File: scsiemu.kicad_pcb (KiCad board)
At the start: 2 copper layers, 65 x 41.7 mm, 38 parts, among them J1 RasPi, J2 SCSI, J3 USB_POWER, J4 POWER 5V, J5 I2C, U1 74LS641-1, U2 74LS641-1, U3 74LS641-1, U4 74LS641-1

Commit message: update libs update PCBs update schematic
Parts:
- removed REF** (x6): MountingHole_2.2mm_M2, MountingHole:MountingHole_2.2mm_M2
- removed RN10, RN5, RN7, RN8: 220, Resistor_SMD:R_Cat16-8
- removed RN11, RN6, RN9: 330, Resistor_SMD:R_Cat16-8
- added C10: 10u, Capacitor_SMD:C_1206_3216Metric_Pad1.42x1.75mm_HandSolder, B.Cu at (183.9, 64.0)
- added C11: 10u, Capacitor_SMD:C_1206_3216Metric_Pad1.42x1.75mm_HandSolder, B.Cu at (155.6, 64.3)
- added C6: 10u, Capacitor_SMD:C_1206_3216Metric_Pad1.42x1.75mm_HandSolder, F.Cu at (176.8, 49.1)
- added C7: 2.2u, Capacitor_SMD:C_0603_1608Metric_Pad1.05x0.95mm_HandSolder, F.Cu at (176.4, 61.6)
- added C8: 10u, Capacitor_SMD:C_1206_3216Metric_Pad1.42x1.75mm_HandSolder, F.Cu at (165.7, 48.0)
- added C9: 2.2u, Capacitor_SMD:C_0603_1608Metric_Pad1.05x0.95mm_HandSolder, F.Cu at (173.2, 51.7)
- added D2: SBD, local_lib:D_SOD-123_HandSoldering, F.Cu at (120.1, 57.2)
- added J6: AT Power 5V (171826-4), local_lib:Molex_171826-4, F.Cu at (119.6, 49.8)
- added J7: I2C Ext, Connector_JST:JST_XH_B6B-XH-A_1x06_P2.50mm_Vertical, F.Cu at (174.0, 68.8)
- added J8: AT Power 5V (641737-1), local_lib:TE_641737-1, F.Cu at (122.2, 35.4)
- added LED2: LED ACT, LED_SMD:LED_0603_1608Metric_Pad1.05x0.95mm_HandSolder, F.Cu at (183.7, 68.4)
- added MH1: Raspi Mount, MountingHole:MountingHole_2.2mm_M2, F.Cu at (138.5, 100.2)
- added MH10: Raspi Mount, MountingHole:MountingHole_2.2mm_M2, F.Cu at (138.5, 126.2)
- added MH2: Raspi Mount, MountingHole:MountingHole_2.2mm_M2, F.Cu at (138.5, 77.2)
- added MH3: Raspi Mount, MountingHole:MountingHole_2.2mm_M2, F.Cu at (196.5, 77.2)
- added MH4: Raspi Mount, MountingHole:MountingHole_2.2mm_M2, F.Cu at (196.5, 100.2)
- added MH5: HDD Mount, MountingHole:MountingHole_3.5mm, F.Cu at (112.0, 57.0)
- added MH6: HDD Mount, MountingHole:MountingHole_3.5mm, F.Cu at (112.0, 133.2)
- added MH7: HDD Mount, MountingHole:MountingHole_3.5mm, F.Cu at (207.2, 57.0)
- added MH8: HDD Mount, MountingHole:MountingHole_3.5mm, F.Cu at (207.2, 133.2)
- added MH9: Raspi Mount, MountingHole:MountingHole_2.2mm_M2, F.Cu at (196.5, 126.2)
- added R2: 2.2k, Resistor_SMD:R_0603_1608Metric_Pad1.05x0.95mm_HandSolder, F.Cu at (125.3, 59.9)
- added R3: 2.7k, Resistor_SMD:R_0603_1608Metric_Pad1.05x0.95mm_HandSolder, F.Cu at (125.4, 57.8)
- added U5: DS2105Z, Package_SO:SOIC-16_3.9x9.9mm_P1.27mm, F.Cu at (181.6, 56.6)
- added U6: DS2105Z, Package_SO:SOIC-16_3.9x9.9mm_P1.27mm, F.Cu at (168.0, 55.9)
- added U7: TL2218-285, Package_SO:TSSOP-20_4.4x6.5mm_P0.65mm, B.Cu at (190.1, 66.5)
- added U8: TL2218-285, Package_SO:TSSOP-20_4.4x6.5mm_P0.65mm, B.Cu at (147.2, 64.3)
- C1, C4: value 0.1u JB -> 0.1u; moved to F.Cu
- C2: value 0.1u JB -> 0.1u
- C3: value 0.1u JIS B -> 0.1u; moved to F.Cu
- C5: value 10u JB -> 10u; moved to F.Cu
- D1: footprint cd_device:D_SOD-123_HandSoldering -> local_lib:D_SOD-123_HandSoldering; moved to F.Cu
- F1, FL1, FL2, R1, U1, U2, U3, U4: moved to F.Cu
- F2: value 1A -> 2A; moved to F.Cu
- J2: footprint local_lib:DSUB50P -> Connector_PinHeader_2.54mm:PinHeader_2x25_P2.54mm_Horizontal
- J4: footprint Connector_JST:JST_PH_S2B-PH-K_1x02_P2.00mm_Horizontal -> Connector_JST:JST_XH_B2B-XH-A_1x02_P2.50mm_Vertical
- J5: value I2C -> POWER 5V; footprint Connector_JST:JST_PH_S3B-PH-K_1x03_P2.00mm_Horizontal -> Connector_JST:JST_XH_B2B-XH-A_1x02_P2.50mm_Vertical
- moved J1 85.3 mm to (191.6, 78.4), turned to 270 degrees
- moved LED1 83.9 mm to (180.1, 67.1), turned to 270 degrees
- moved R1 80.5 mm to (179.5, 64.2), turned to 90 degrees
- moved FL1 78.2 mm to (191.8, 83.1), turned to 270 degrees
- moved C5 55.8 mm to (162.1, 104.4), turned to 270 degrees
- moved U1 55.4 mm to (193.3, 116.6), turned to 0 degrees
- moved U2 55.0 mm to (186.4, 100.1), turned to 0 degrees
- moved C2 53.7 mm to (191.3, 91.7), turned to 90 degrees
- moved C1 50.1 mm to (198.1, 108.0), turned to 90 degrees
- moved J3 46.8 mm to (124.8, 135.6), turned to 0 degrees
- moved RN1 41.8 mm to (173.2, 101.3), turned to 180 degrees
- moved RN4 39.4 mm to (175.8, 116.1), turned to 180 degrees
- moved C3 34.6 mm to (148.3, 103.9), turned to 90 degrees
- moved F2 33.8 mm to (126.5, 66.7)
- moved RN3 33.0 mm to (153.4, 91.4), turned to 0 degrees
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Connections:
- D1 pad 2: VCC -> /5V_DC
- F2 pad 1: Net-(F2-Pad1) -> /5V_DC
- F2 pad 2: Net-(F2-Pad2) -> Net-(D2-Pad1)
- FL2 pad 3: Net-(F2-Pad1) -> /5V_DC
- J1 pad 2: Net-(F2-Pad1) -> /5V_DC
- J1 pad 21: Net-(J1-Pad21) -> /AT_POWER_ON
- J1 pad 27: Net-(J1-Pad27) -> /EXT1
- J1 pad 28: Net-(J1-Pad28) -> /EXT2
- J1 pad 4: Net-(F2-Pad1) -> /5V_DC
- J2 pad 10: GND -> /S_D4
- J2 pad 12: GND -> /S_D5
- J2 pad 14: GND -> /S_D6
- J2 pad 16: GND -> /S_D7
- J2 pad 18: GND -> /S_DP
- J2 pad 2: GND -> /S_D0
- J2 pad 25: GND -> Net-(J2-Pad25)
- J2 pad 26: /S_D0 -> Net-(F1-Pad1)
- J2 pad 27: /S_D1 -> GND
- J2 pad 28: /S_D2 -> GND
- J2 pad 29: /S_D3 -> GND
- J2 pad 30: /S_D4 -> GND
- J2 pad 31: /S_D5 -> GND
- J2 pad 32: /S_D6 -> /S_ATN
- J2 pad 33: /S_D7 -> GND
- J2 pad 34: /S_DP -> Net-(J2-Pad34)
- J2 pad 36: GND -> /S_BSY
- J2 pad 38: Net-(F1-Pad1) -> /S_ACK
- J2 pad 4: GND -> /S_D1
- J2 pad 40: GND -> /S_RST
- J2 pad 41: Net-(J2-Pad41) -> GND
- J2 pad 42: GND -> /S_MSG
- J2 pad 43: Net-(J2-Pad43) -> GND
- J2 pad 44: Net-(J2-Pad44) -> /S_SEL
- J2 pad 45: Net-(J2-Pad45) -> GND
- J2 pad 46: Net-(J2-Pad46) -> /S_CD
- J2 pad 47: Net-(J2-Pad47) -> GND
- J2 pad 48: Net-(J2-Pad48) -> /S_REQ
- J2 pad 49: Net-(J2-Pad49) -> GND
- J2 pad 50: Net-(J2-Pad50) -> /S_IO
- J2 pad 6: GND -> /S_D2
- J2 pad 8: GND -> /S_D3
- J3 pad 1: Net-(F2-Pad2) -> Net-(D2-Pad1)
- J4 pad 1: Net-(F2-Pad2) -> GND
- J4 pad 2: GND -> Net-(D2-Pad1)
- J5 pad 2: /I2C_SCL -> Net-(D2-Pad1)
- RN1 pad 3: Net-(RN1-Pad3) -> /SEL
- RN1 pad 4: Net-(RN1-Pad4) -> /RST
- RN1 pad 5: /ATN -> Net-(RN1-Pad5)
- RN1 pad 6: /RST -> Net-(RN1-Pad6)
- RN1 pad 8: /SEL -> /ATN
- RN2 pad 8: /DP -> /D0
- RN3 pad 1: /D3 -> /DP
- RN3 pad 2: /D1 -> /D7
- RN3 pad 3: /D0 -> /D6
- RN3 pad 4: /D2 -> /D5
- RN3 pad 5: /D5 -> /D4
- RN3 pad 6: /D6 -> /D3
- RN3 pad 7: /D4 -> /D2
- RN3 pad 8: /D7 -> /D1
- RN4 pad 4: /BSY -> /IO
- RN4 pad 5: /MSG -> /REQ
- RN4 pad 7: /REQ -> /MSG
- RN4 pad 8: /IO -> /BSY
- U1 pad 14: Net-(J2-Pad43) -> /S_IO
- U1 pad 15: Net-(J2-Pad46) -> /S_REQ
- U1 pad 16: Net-(J2-Pad48) -> /S_CD
- U1 pad 17: Net-(J2-Pad49) -> /S_MSG
- U1 pad 18: Net-(J2-Pad50) -> /S_BSY
- U1 pad 2: /IO -> /BSY
- U1 pad 3: /REQ -> /MSG
- U1 pad 5: /MSG -> /REQ
- U1 pad 6: /BSY -> /IO
- U2 pad 13: Net-(RN5-Pad3) -> /S_SEL
- U2 pad 14: Net-(RN5-Pad4) -> /S_RST
- U2 pad 15: Net-(J2-Pad41) -> Net-(U2-Pad15)
- U2 pad 16: Net-(J2-Pad45) -> Net-(U2-Pad16)
- U2 pad 17: Net-(J2-Pad44) -> /S_ACK
- U2 pad 18: Net-(J2-Pad47) -> /S_ATN
- U2 pad 2: /SEL -> /ATN
- U2 pad 4: /RST -> Net-(RN1-Pad6)
- U2 pad 5: /ATN -> Net-(RN1-Pad5)
- U2 pad 6: Net-(RN1-Pad4) -> /RST
- U2 pad 7: Net-(RN1-Pad3) -> /SEL
- U3 pad 11: /DP -> /D0
- U3 pad 9: /S_DP -> /S_D0
- U4 pad 11: /D7 -> /D1
- U4 pad 12: /D4 -> /D2
- U4 pad 13: /D6 -> /D3
- U4 pad 14: /D5 -> /D4
- U4 pad 15: /D2 -> /D5
- U4 pad 16: /D0 -> /D6
- U4 pad 17: /D1 -> /D7
- U4 pad 18: /D3 -> /DP
- U4 pad 2: /S_D3 -> /S_DP
- U4 pad 3: /S_D1 -> /S_D7
- U4 pad 4: /S_D0 -> /S_D6
- U4 pad 5: /S_D2 -> /S_D5
- U4 pad 6: /S_D5 -> /S_D4
- U4 pad 7: /S_D6 -> /S_D3
- U4 pad 8: /S_D4 -> /S_D2
- U4 pad 9: /S_D7 -> /S_D1
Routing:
- net /S_BSY: track 0.00 -> 120.0 mm, vias 0 -> 3
- net VCC: track 132.8 -> 14.9 mm, vias 4 -> 0
- net /S_REQ: track 0.00 -> 111.5 mm, vias 0 -> 2
- net /S_IO: track 0.00 -> 109.5 mm, vias 0 -> 2
- net /S_CD: track 0.00 -> 102.4 mm, vias 0 -> 1
- net /S_SEL: track 0.00 -> 101.5 mm, vias 0 -> 2
- net GND: track 100.9 -> 0.00 mm, vias 55 -> 33
- net /S_ACK: track 0.00 -> 99.8 mm, vias 0 -> 2
- net /S_MSG: track 0.00 -> 99.7 mm, vias 0 -> 1
- net /S_RST: track 0.00 -> 94.3 mm, vias 0 -> 1
- net /S_ATN: track 0.00 -> 89.8 mm, vias 0 -> 1
- net Net-(D2-Pad1): track 0.00 -> 81.3 mm
- net /5V_DC: track 0.00 -> 70.3 mm
- net /S_D0: track 12.7 -> 82.5 mm, vias 1 -> 0
- net /DTD: track 91.3 -> 26.3 mm, vias 3 -> 0
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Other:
- board size 65 x 41.7 mm -> 100 x 99 mm
- net class Default: clearance 0.2 -> 0.25; via_drill 0.4 -> 0.3
- net class LV added: clearance 0.2, trace_width 0.2, via_dia 0.7, via_drill 0.3
- rule trace_clearance: 0.2 -> 0.25
- board text added: "ATX POWER 5V"
- board text removed: "*"
- board text removed: "+"
- board text removed: "D+"
- board text removed: "D-"
- board text removed: "GND"
- board text removed: "ID"
- board text removed: "SDA|SCL|G"

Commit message: update track
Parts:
- added R4: 1k, Resistor_SMD:R_0603_1608Metric_Pad1.05x0.95mm_HandSolder, F.Cu at (128.0, 52.9)
- LED1: value LED ACT -> LED PWR; footprint LED_THT:LED_D3.0mm -> LED_SMD:LED_0603_1608Metric_Pad1.05x0.95mm_HandSolder
- moved LED1 51.6 mm to (130.4, 52.9)
- moved C5 9.88 mm to (152.2, 103.1), turned to 90 degrees
- moved LED2 2.69 mm to (181.0, 68.5)
- moved RN2 1.35 mm to (151.0, 111.4)
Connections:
- LED1 pad 2: /ACT -> /5V_DC
- LED2 pad 1: Net-(LED1-Pad1) -> Net-(LED2-Pad1)
- R1 pad 1: Net-(LED1-Pad1) -> Net-(LED2-Pad1)
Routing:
- net VCC: track 14.9 -> 200.3 mm, vias 0 -> 2
- net VEE: track 0.00 -> 155.6 mm, vias 0 -> 5
- net /RST: track 0.00 -> 74.1 mm
- net /D0: track 0.00 -> 72.1 mm, vias 0 -> 4
- net /BSY: track 0.00 -> 71.8 mm, vias 0 -> 2
- net /IO: track 0.00 -> 68.3 mm, vias 0 -> 2
- net /TAD: track 0.00 -> 60.4 mm, vias 0 -> 2
- net /MSG: track 0.00 -> 57.8 mm, vias 0 -> 2
- net /CD: track 0.00 -> 56.9 mm, vias 0 -> 2
- net /ACK: track 0.00 -> 56.9 mm, vias 0 -> 2
- net /REQ: track 0.00 -> 55.0 mm
- net /D4: track 0.00 -> 50.5 mm, vias 0 -> 1
- net /DTD: track 26.3 -> 74.6 mm, vias 0 -> 1
- net /D5: track 0.00 -> 47.9 mm, vias 0 -> 1
- net /ATN: track 0.00 -> 46.5 mm
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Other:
- board text added: "SCSI emu v1"
- board text removed: "SCSI"

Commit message: add tracks more
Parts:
- moved C11 18.9 mm to (149.6, 46.4), turned to 180 degrees
- moved U8 13.2 mm to (148.4, 51.1), turned to 180 degrees
- moved C8 1.88 mm to (167.6, 47.8)
- moved C6 1.83 mm to (178.5, 48.5)
- moved C9 1.04 mm to (173.2, 50.6)
- moved U6 0.32 mm to (168.1, 55.6)
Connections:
- U6 pad 11: Net-(U6-Pad11) -> /S_D0
- U6 pad 12: Net-(U6-Pad12) -> /S_D2
- U6 pad 13: Net-(U6-Pad13) -> /S_D4
- U6 pad 14: Net-(U6-Pad14) -> /S_D7
- U6 pad 2: Net-(U6-Pad2) -> /S_DP
- U6 pad 3: Net-(U6-Pad3) -> /S_D6
- U6 pad 4: Net-(U6-Pad4) -> /S_D5
- U6 pad 5: Net-(U6-Pad5) -> /S_D3
- U6 pad 6: Net-(U6-Pad6) -> /S_D1
- U8 pad 13: Net-(U8-Pad13) -> /S_D3
- U8 pad 14: Net-(U8-Pad14) -> /S_D2
- U8 pad 16: Net-(U8-Pad16) -> /S_D1
- U8 pad 17: Net-(U8-Pad17) -> /S_D0
- U8 pad 4: Net-(U8-Pad4) -> /S_DP
- U8 pad 5: Net-(U8-Pad5) -> /S_D7
- U8 pad 6: Net-(U8-Pad6) -> /S_D6
- U8 pad 7: Net-(U8-Pad7) -> /S_D5
- U8 pad 8: Net-(U8-Pad8) -> /S_D4
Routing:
- net VCC: track 200.3 -> 283.8 mm, vias 2 -> 4
- net /S_D0: track 82.5 -> 128.6 mm, vias 0 -> 2
- net GND: track 30.4 -> 72.1 mm, vias 121 -> 179
- net /S_D2: track 62.4 -> 99.8 mm, vias 0 -> 2
- net /S_D1: track 63.1 -> 96.8 mm, vias 0 -> 2
- net /S_D4: track 61.2 -> 86.0 mm, vias 0 -> 2
- net /S_D7: track 59.8 -> 83.5 mm, vias 0 -> 2
- net /S_D3: track 61.9 -> 84.4 mm, vias 0 -> 2
- net /AT_POWER_ON: track 41.3 -> 61.8 mm, vias 1 -> 3
- net /S_DP: track 59.3 -> 76.3 mm, vias 0 -> 1
- net /S_D5: track 60.5 -> 76.7 mm, vias 0 -> 2
- net /S_D6: track 60.1 -> 75.4 mm, vias 0 -> 2
- net Net-(C9-Pad1): track 0.00 -> 13.1 mm
- net /5V_DC: track 111.9 -> 118.7 mm
- net /AT_5V_DC: track 20.2 -> 25.0 mm
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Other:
- board text added: "SCSI emu v2"
- board text removed: "SCSI emu v1"

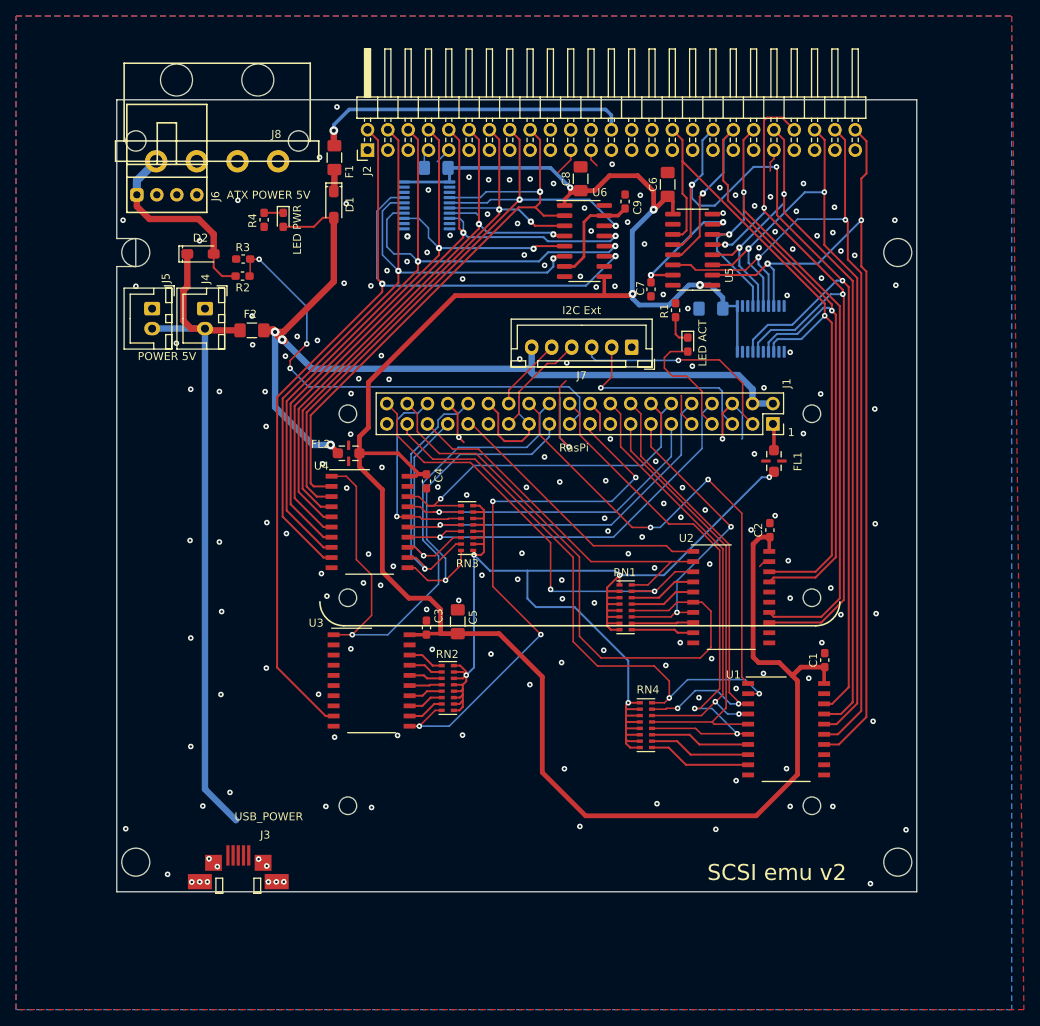
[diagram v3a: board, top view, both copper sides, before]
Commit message: update PCB outlines
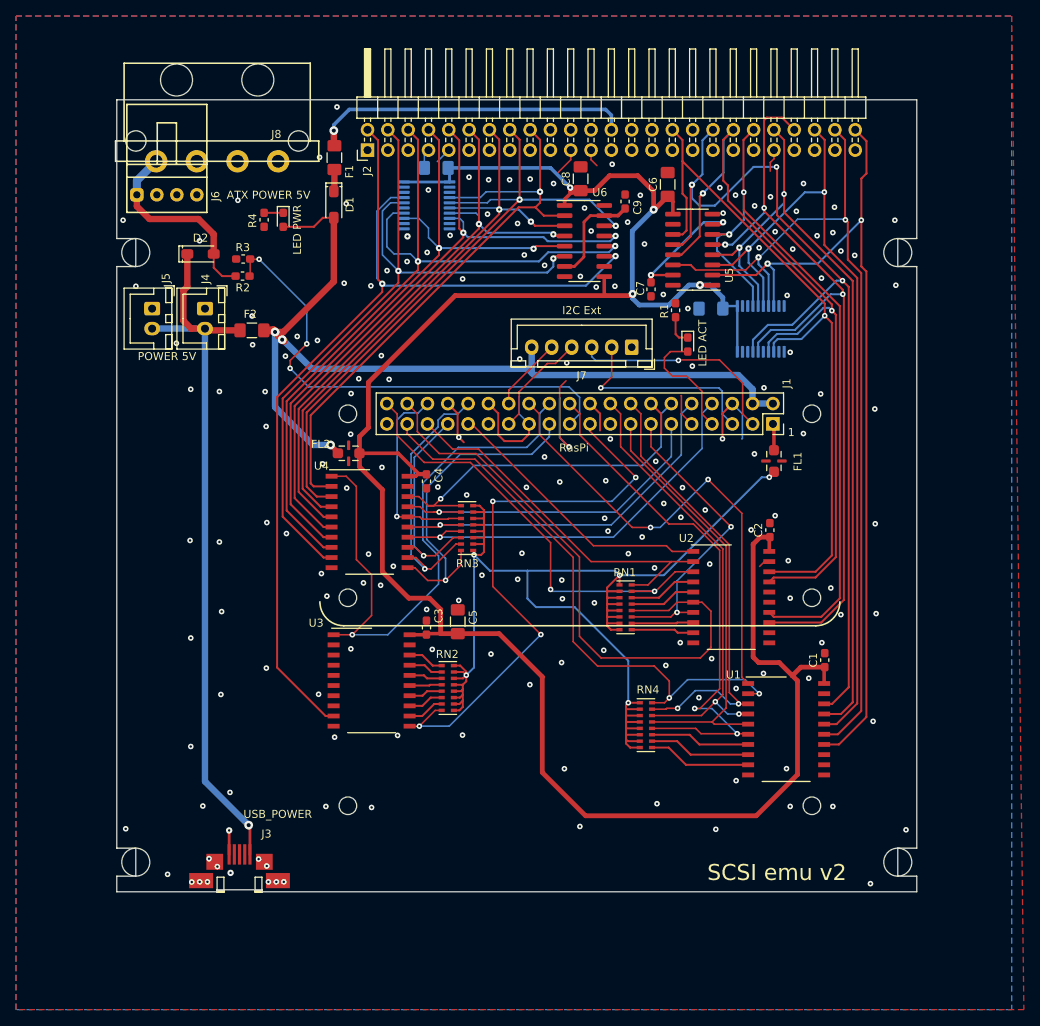
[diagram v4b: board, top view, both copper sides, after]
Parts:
- moved J3 0.20 mm to (125.0, 135.5)
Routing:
- net Net-(D2-Pad1): track 85.8 -> 90.8 mm, vias 0 -> 1
- net GND: track 72.1 -> 75.1 mm, vias 179 -> 181
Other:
- outline, holes or cut-outs redrawn

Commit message: update outline
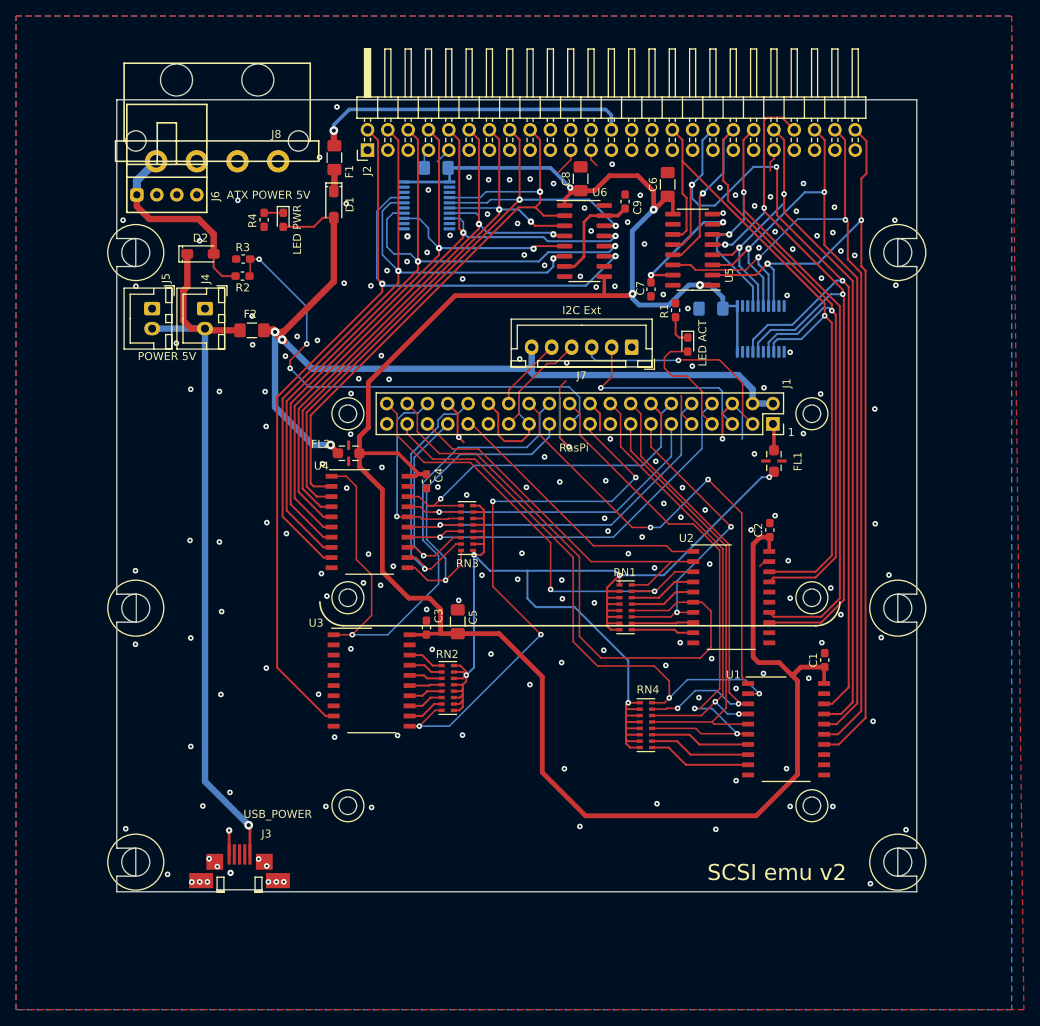
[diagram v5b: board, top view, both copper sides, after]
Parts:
- added MH11: HDD Mount, MountingHole:MountingHole_3.5mm, F.Cu at (112.0, 101.5)
- added MH12: HDD Mount, MountingHole:MountingHole_3.5mm, F.Cu at (207.2, 101.5)
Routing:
- net GND: vias 181 -> 184
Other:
- outline, holes or cut-outs redrawn

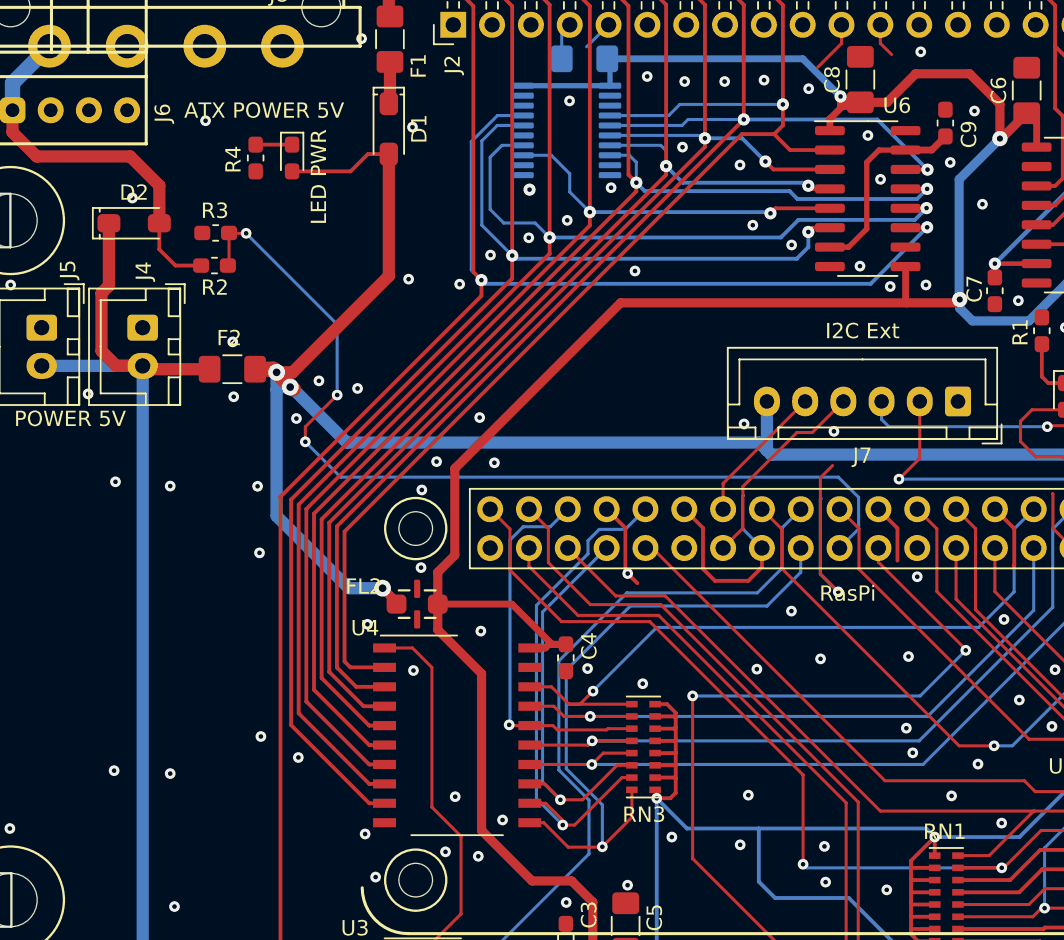
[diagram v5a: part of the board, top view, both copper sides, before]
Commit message: add mounting holes
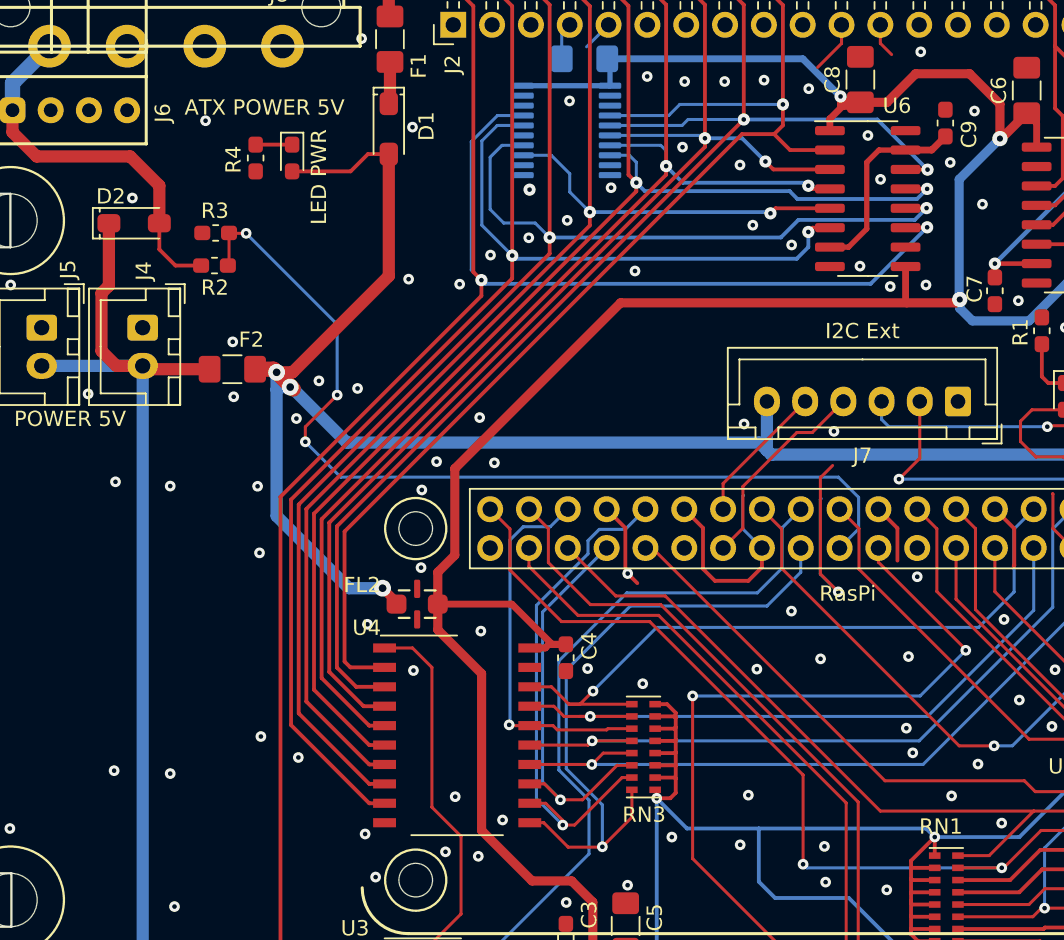
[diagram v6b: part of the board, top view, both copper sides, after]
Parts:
- F1: value 1A -> 750mA ~~ 1A (0ZCJ0075FF2E)
- F2: value 2A -> 2A (0685T2000-01)
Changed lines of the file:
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@@
     (tags D_SOD-123_HandSoldering)
     (attr smd)
-    (fp_text reference D2 (at 0 -2) (layer F.SilkS)
+    (fp_text reference D2 (at -1.524 -1.7526) (layer F.SilkS)
       (effects (font (size 1 1) (thickness 0.15)))
     )
@@
     (tags D_SOD-123_HandSoldering)
     (attr smd)
-    (fp_text reference D1 (at 0 -2 90) (layer F.SilkS)
+    (fp_text reference D1 (at -0.1778 -2.4638 90) (layer F.SilkS)
       (effects (font (size 1 1) (thickness 0.15)))
     )
@@
     (tags "S0-20 ")
     (attr smd)
-    (fp_text reference U4 (at -6.0198 -7.0104 180) (layer F.SilkS)
+    (fp_text reference U4 (at -5.9182 -7.0358 180) (layer F.SilkS)
       (effects (font (size 1 1) (thickness 0.15)))
     )
@@
       (effects (font (size 1 1) (thickness 0.15)))
     )
-    (fp_text value 1A (at 0 1.82 270) (layer F.Fab)
+    (fp_text value "750mA ~~ 1A (0ZCJ0075FF2E)" (at 0 1.82 270) (layer F.Fab)
       (effects (font (size 1 1) (thickness 0.15)))
     )
@@
   (module cd_device:NFM21PC (layer F.Cu)
     (at 138.6078 82.0928 180)
-    (fp_text reference FL2 (at 3.4925 1.143) (layer F.SilkS)
+    (fp_text reference FL2 (at 3.6068 1.2446) (layer F.SilkS)
       (effects (font (size 1 1) (thickness 0.15)))
     )
@@
     (tags "SMT resistor net Bourns CAT16 series 8 way")
     (attr smd)
-    (fp_text reference RN1 (at 0.1016 4.3561) (layer F.SilkS)
+    (fp_text reference RN1 (at 0.3556 4.699) (layer F.SilkS)
       (effects (font (size 1 1) (thickness 0.15)))
     )
@@
     (tags "resistor handsolder")
     (attr smd)
-    (fp_text reference F2 (at 0.2032 2.032 180) (layer F.SilkS)
-      (effects (font (size 1 1) (thickness 0.15)))
-    )
-    (fp_text value 2A (at 0 1.82 180) (layer F.Fab)
+    (fp_text reference F2 (at -1.2446 1.9304 180) (layer F.SilkS)
+      (effects (font (size 1 1) (thickness 0.15)))
+    )
+    (fp_text value "2A (0685T2000-01)" (at 0 1.82 180) (layer F.Fab)
       (effects (font (size 1 1) (thickness 0.15)))
     )
@@
   (gr_line (start 112.1029 51.2191) (end 113.6904 52.8066) (layer F.Mask) (width 0.9))
   (gr_line (start 112.1156 49.6062) (end 112.1156 51.2191) (layer F.Mask) (width 0.9))
-  (gr_text "ATX POWER 5V" (at 128.6002 49.8094) (layer F.SilkS)
+  (gr_text "ATX POWER 5V" (at 128.6256 49.6062) (layer F.SilkS)
     (effects (font (size 1 1) (thickness 0.15)))
   )
